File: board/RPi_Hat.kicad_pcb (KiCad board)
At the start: 2 copper layers, 65 x 56.5 mm, 33 parts, among them IC1 ATMEGA328P-P, IC2 RFM69HW, J1 RPi_GPIO, P6 SW_CONN, P7 CONN_01X01, Q1 BSS138_GSD, SW1 SWITCH, Y1 16MHz

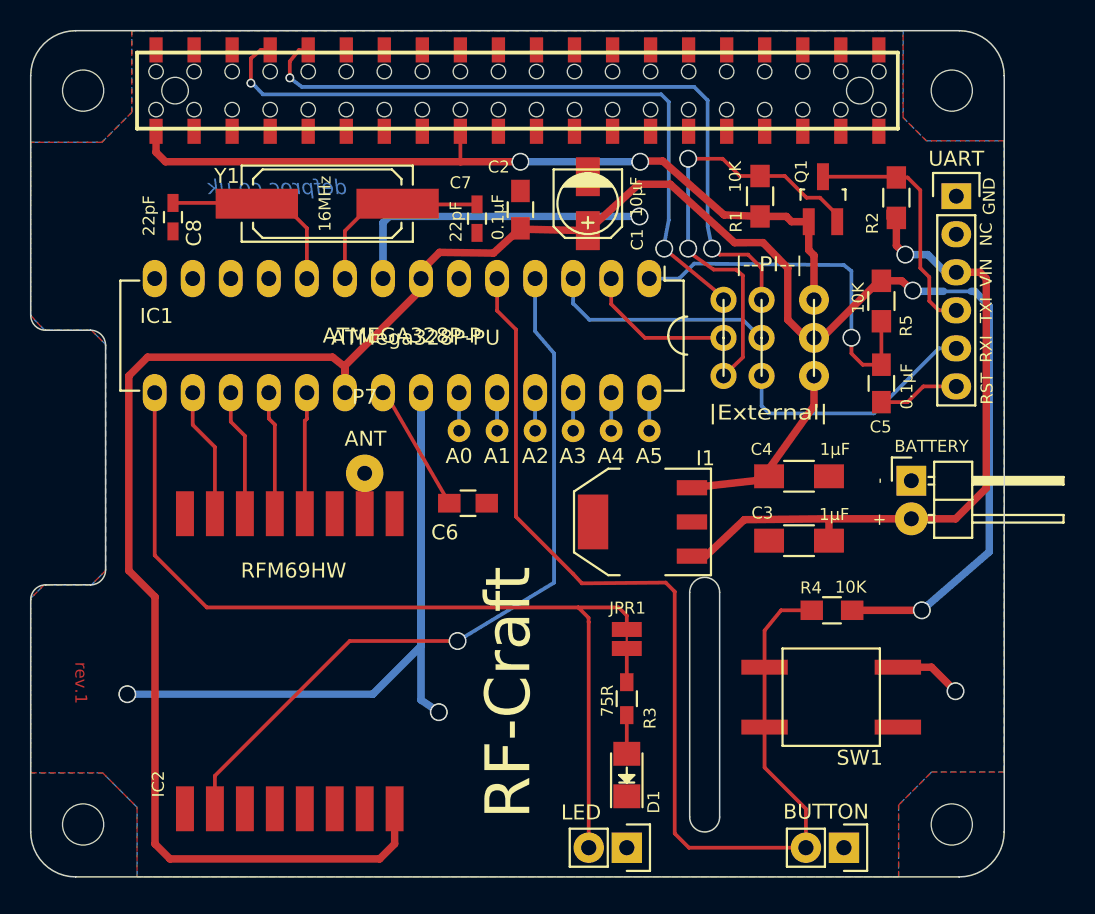
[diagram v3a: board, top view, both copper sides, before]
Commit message: checked vias and rerouted a 3.3V line. Ready for manufacture
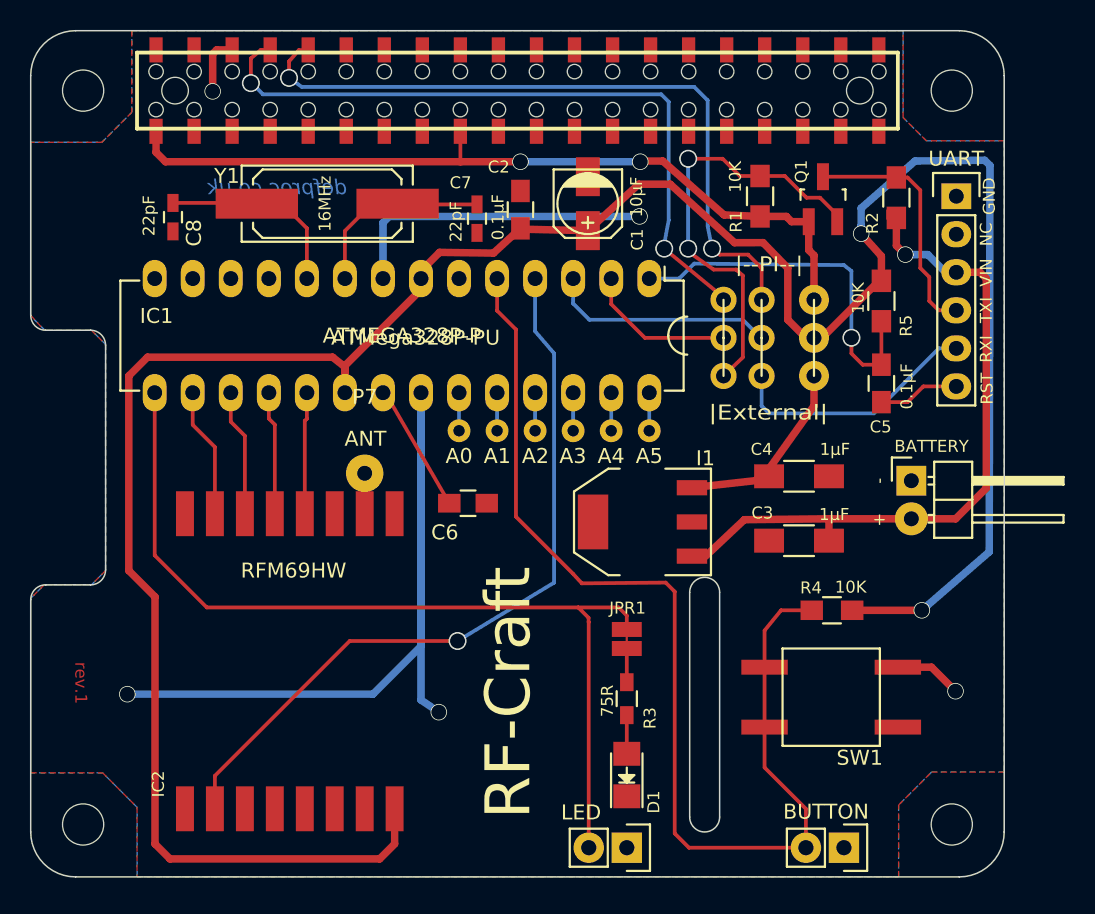
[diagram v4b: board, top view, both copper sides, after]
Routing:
- net V3.3: track 154.0 -> 170.9 mm
- net GND: track 85.4 -> 89.3 mm, vias 4 -> 5
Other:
- net class BUS: via_dia 1.2 -> 1.1
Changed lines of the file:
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@@
     (thickness 1.6)
     (drawings 52)
-    (tracks 257)
+    (tracks 259)
     (zones 0)
     (modules 33)
@@
     (0 F.Cu signal)
     (31 B.Cu signal)
-    (32 B.Adhes user)
+    (32 B.Adhes user hide)
     (33 F.Adhes user)
-    (34 B.Paste user)
+    (34 B.Paste user hide)
     (35 F.Paste user)
-    (36 B.SilkS user)
+    (36 B.SilkS user hide)
     (37 F.SilkS user)
-    (38 B.Mask user)
+    (38 B.Mask user hide)
     (39 F.Mask user)
     (40 Dwgs.User user)
@@
     (visible_elements 7FFEFFFF)
     (pcbplotparams
-      (layerselection 0x00030_80000001)
+      (layerselection 0x010ff_80000001)
       (usegerberextensions false)
       (excludeedgelayer true)
@@
       (drillshape 0)
       (scaleselection 1)
-      (outputdirectory meta/))
+      (outputdirectory gerbers/))
   )
   (net 0 "")
@@
     (clearance 0.2)
     (trace_width 0.5)
-    (via_dia 1.2)
+    (via_dia 1.1)
     (via_drill 1)
     (uvia_dia 0.6)
@@
   (gr_line (start 141.2 47.45) (end 141.2 97.95) (angle 90) (layer Edge.Cuts) (width 0.1))
   (gr_line (start 79.2 44.45) (end 138.2 44.45) (angle 90) (layer Edge.Cuts) (width 0.1))
-  (via (at 135.1 61.8) (size 1.2) (drill 1) (layers F.Cu B.Cu) (net 29))
-  (segment (start 135.05 61.75) (end 135.1 61.8) (width 0.5) (layer F.Cu) (net 29))
-  (segment (start 133 61.15) (end 134.35 61.15) (width 0.5) (layer F.Cu) (net 29))
-  (segment (start 134.35 61.15) (end 135.05 61.75) (width 0.5) (layer F.Cu) (net 29))
+  (segment (start 140.25 53.45) (end 139.9 53.1) (width 0.5) (layer B.Cu) (net 29))
+  (via (at 135.7 83.15) (size 1.1) (drill 1) (layers F.Cu B.Cu) (net 29))
+  (segment (start 135.7 83.15) (end 140.2 79.25) (width 0.5) (layer B.Cu) (net 29))
+  (segment (start 140.2 79.25) (end 140.25 53.45) (width 0.5) (layer B.Cu) (net 29))
   (segment (start 131.05 83.15) (end 135.7 83.15) (width 0.5) (layer F.Cu) (net 29) (status 10))
-  (via (at 135.7 83.15) (size 1.2) (drill 1) (layers F.Cu B.Cu) (net 29))
-  (segment (start 135.7 83.15) (end 140.2 79.25) (width 0.5) (layer B.Cu) (net 29))
-  (segment (start 140.2 79.25) (end 140.2 62.85) (width 0.5) (layer B.Cu) (net 29))
-  (segment (start 140.2 62.85) (end 139.25 61.860417) (width 0.5) (layer B.Cu) (net 29))
-  (segment (start 139.25 61.860417) (end 139 61.85) (width 0.5) (layer B.Cu) (net 29))
-  (segment (start 137.15 61.85) (end 135.15 61.85) (width 0.5) (layer B.Cu) (net 29))
-  (segment (start 139 61.85) (end 137.15 61.85) (width 0.25) (layer B.Cu) (net 29))
-  (segment (start 135.15 61.85) (end 135.1 61.8) (width 0.5) (layer B.Cu) (net 29))
-  (segment (start 135.1 61.8) (end 135.1 61.8) (width 0.25) (layer B.Cu) (net 29))
+  (segment (start 133 59.5) (end 133 61.15) (width 0.5) (layer F.Cu) (net 29))
+  (segment (start 131.65 58) (end 133 59.5) (width 0.5) (layer F.Cu) (net 29))
+  (via (at 131.65 58) (size 1.1) (drill 1) (layers F.Cu B.Cu) (net 29))
+  (segment (start 131.65 57.45) (end 131.65 58) (width 0.5) (layer B.Cu) (net 29))
+  (segment (start 135.25 53.15) (end 131.65 56.3) (width 0.5) (layer B.Cu) (net 29))
+  (segment (start 131.65 56.3) (end 131.65 57.45) (width 0.5) (layer B.Cu) (net 29))
+  (segment (start 139.9 53.1) (end 135.25 53.15) (width 0.5) (layer B.Cu) (net 29))
   (segment (start 97.18 68.62) (end 97.18 66.9) (width 0.5) (layer F.Cu) (net 29))
   (segment (start 100.5 98.75) (end 100.5 96.4) (width 0.5) (layer F.Cu) (net 29))
@@
   (segment (start 102.26 61.74) (end 97.18 66.82) (width 0.5) (layer F.Cu) (net 29))
   (segment (start 97.18 66.82) (end 97.18 68.62) (width 0.5) (layer F.Cu) (net 29))
+  (segment (start 89.65 45.7322) (end 88.6178 45.7322) (width 0.5) (layer F.Cu) (net 30))
+  (via (at 88.35 48.5) (size 1.1) (drill 1) (layers F.Cu B.Cu) (net 30))
+  (segment (start 88.35 46) (end 88.35 48.5) (width 0.5) (layer F.Cu) (net 30))
+  (segment (start 88.6178 45.7322) (end 88.35 46) (width 0.5) (layer F.Cu) (net 30))
   (segment (start 134.1 86.95) (end 136.35 86.95) (width 0.5) (layer F.Cu) (net 30))
-  (via (at 137.95 88.55) (size 1.2) (drill 1) (layers F.Cu B.Cu) (net 30))
+  (via (at 137.95 88.55) (size 1.1) (drill 1) (layers F.Cu B.Cu) (net 30))
   (segment (start 136.35 86.95) (end 137.95 88.55) (width 0.5) (layer F.Cu) (net 30))
   (segment (start 99.72 61) (end 99.72 57.27) (width 0.5) (layer B.Cu) (net 30))
-  (via (at 116.85 56.85) (size 1.2) (drill 1) (layers F.Cu B.Cu) (net 30))
+  (via (at 116.85 56.85) (size 1.1) (drill 1) (layers F.Cu B.Cu) (net 30))
   (segment (start 100.14 56.85) (end 116.85 56.85) (width 0.5) (layer B.Cu) (net 30))
   (segment (start 99.72 57.27) (end 100.14 56.85) (width 0.5) (layer B.Cu) (net 30))
   (segment (start 102.26 68.62) (end 102.26 85.54) (width 0.5) (layer B.Cu) (net 30))
-  (via (at 82.65 88.75) (size 1.2) (drill 1) (layers F.Cu B.Cu) (net 30))
+  (via (at 82.65 88.75) (size 1.1) (drill 1) (layers F.Cu B.Cu) (net 30))
   (segment (start 99.05 88.75) (end 82.65 88.75) (width 0.5) (layer B.Cu) (net 30))
   (segment (start 102.26 85.54) (end 99.05 88.75) (width 0.5) (layer B.Cu) (net 30))
   (segment (start 102.26 68.62) (end 102.26 89.14) (width 0.5) (layer B.Cu) (net 30))
   (segment (start 102.26 89.14) (end 103.45 89.95) (width 0.5) (layer B.Cu) (net 30))
-  (via (at 103.45 89.95) (size 1.2) (drill 1) (layers F.Cu B.Cu) (net 30))
+  (via (at 103.45 89.95) (size 1.1) (drill 1) (layers F.Cu B.Cu) (net 30))
+  (segment (start 138 60.58) (end 139.58 60.58) (width 0.5) (layer F.Cu) (net 31) (status 10))
+  (segment (start 137.96 77.04) (end 135 77.04) (width 0.5) (layer F.Cu) (net 31))
+  (segment (start 140 75) (end 137.96 77.04) (width 0.5) (layer F.Cu) (net 31))
+  (segment (start 140 61) (end 140 75) (width 0.5) (layer F.Cu) (net 31))
+  (segment (start 139.58 60.58) (end 140 61) (width 0.5) (layer F.Cu) (net 31))
   (segment (start 138 60.58) (end 137.28 60.58) (width 0.25) (layer B.Cu) (net 31) (status 30))
   (segment (start 137.28 60.58) (end 136.1 59.4) (width 0.5) (layer B.Cu) (net 31) (status 10))
   (segment (start 136.1 59.4) (end 134.6 59.4) (width 0.5) (layer B.Cu) (net 31))
-  (via (at 134.6 59.4) (size 1.2) (drill 1) (layers F.Cu B.Cu) (net 31))
+  (via (at 134.6 59.4) (size 1.1) (drill 1) (layers F.Cu B.Cu) (net 31))
   (segment (start 134.6 59.4) (end 134 58.8) (width 0.5) (layer F.Cu) (net 31))
   (segment (start 134 58.8) (end 134 56.95) (width 0.5) (layer F.Cu) (net 31))
-  (segment (start 138 60.58) (end 139.58 60.58) (width 0.5) (layer F.Cu) (net 31) (status 10))
-  (segment (start 139.58 60.58) (end 140 61) (width 0.5) (layer F.Cu) (net 31))
-  (segment (start 140 61) (end 140 75) (width 0.5) (layer F.Cu) (net 31))
-  (segment (start 140 75) (end 137.96 77.04) (width 0.5) (layer F.Cu) (net 31))
-  (segment (start 137.96 77.04) (end 135 77.04) (width 0.5) (layer F.Cu) (net 31))
   (segment (start 129.5 78.5) (end 129.5 77.04) (width 0.5) (layer F.Cu) (net 31))
   (segment (start 129.5 77.04) (end 129.5 77) (width 0.25) (layer F.Cu) (net 31))
@@
   (segment (start 117.5 68.62) (end 117.5 71.16) (width 0.25) (layer B.Cu) (net 58))
   (segment (start 98.5 76.7) (end 98.5 74) (width 0.25) (layer F.Cu) (net 65))
-  (segment (start 93.5 47.6) (end 94.3 48.2) (width 0.25) (layer B.Cu) (net 67))
+  (segment (start 93.45 47.6) (end 94.3 48.2) (width 0.25) (layer B.Cu) (net 67))
   (segment (start 94.3 48.2) (end 120.5 48.2) (width 0.25) (layer B.Cu) (net 67))
-  (segment (start 94.1 45.75) (end 93.5 46.5) (width 0.25) (layer F.Cu) (net 67))
-  (segment (start 93.5 46.5) (end 93.5 47.6) (width 0.25) (layer F.Cu) (net 67))
-  (via (at 93.5 47.6) (size 0.6) (drill 0.4) (layers F.Cu B.Cu) (net 67))
+  (segment (start 94.1 45.75) (end 93.45 46.5) (width 0.25) (layer F.Cu) (net 67))
+  (segment (start 93.45 46.5) (end 93.45 47.6) (width 0.25) (layer F.Cu) (net 67))
+  (via (at 93.45 47.6) (size 1.2) (drill 1) (layers F.Cu B.Cu) (net 67))
   (segment (start 94.73 45.7322) (end 94.1 45.75) (width 0.25) (layer F.Cu) (net 67))
   (segment (start 125 60.3) (end 125 62.42) (width 0.25) (layer F.Cu) (net 67))
@@
   (segment (start 92.19 45.7322) (end 91.5678 45.7322) (width 0.25) (layer F.Cu) (net 68))
   (segment (start 90.9 47.95) (end 90.8 47.95) (width 0.25) (layer B.Cu) (net 68))
-  (via (at 90.9 47.95) (size 0.6) (drill 0.4) (layers F.Cu B.Cu) (net 68))
+  (via (at 90.9 47.95) (size 1.2) (drill 1) (layers F.Cu B.Cu) (net 68))
   (segment (start 90.9 46.3) (end 90.9 47.95) (width 0.25) (layer F.Cu) (net 68))
   (segment (start 91.5678 45.7322) (end 90.9 46.3) (width 0.25) (layer F.Cu) (net 68))
@@
   (segment (start 118.396014 53.149827) (end 118.4 53.15416) (width 0.25) (layer F.Cu) (net 69))
   (segment (start 116.9 53.2) (end 117 53.3) (width 0.25) (layer F.Cu) (net 69))
-  (via (at 116.9 53.2) (size 1.2) (drill 1) (layers F.Cu B.Cu) (net 69))
+  (via (at 116.9 53.2) (size 1.1) (drill 1) (layers F.Cu B.Cu) (net 69))
   (segment (start 108.9 53.2) (end 116.9 53.2) (width 0.5) (layer B.Cu) (net 69))
-  (via (at 108.9 53.2) (size 1.2) (drill 1) (layers F.Cu B.Cu) (net 69))
+  (via (at 108.9 53.2) (size 1.1) (drill 1) (layers F.Cu B.Cu) (net 69))
   (segment (start 104.9 53.2) (end 108.9 53.2) (width 0.5) (layer F.Cu) (net 69))
   (segment (start 124.9 56.85) (end 126.65 56.85) (width 0.5) (layer F.Cu) (net 69))
